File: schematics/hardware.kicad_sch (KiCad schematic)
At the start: 4 parts, among them U1 CR2013-MI2120, U2 TXS0108EPW, U3 BMP280

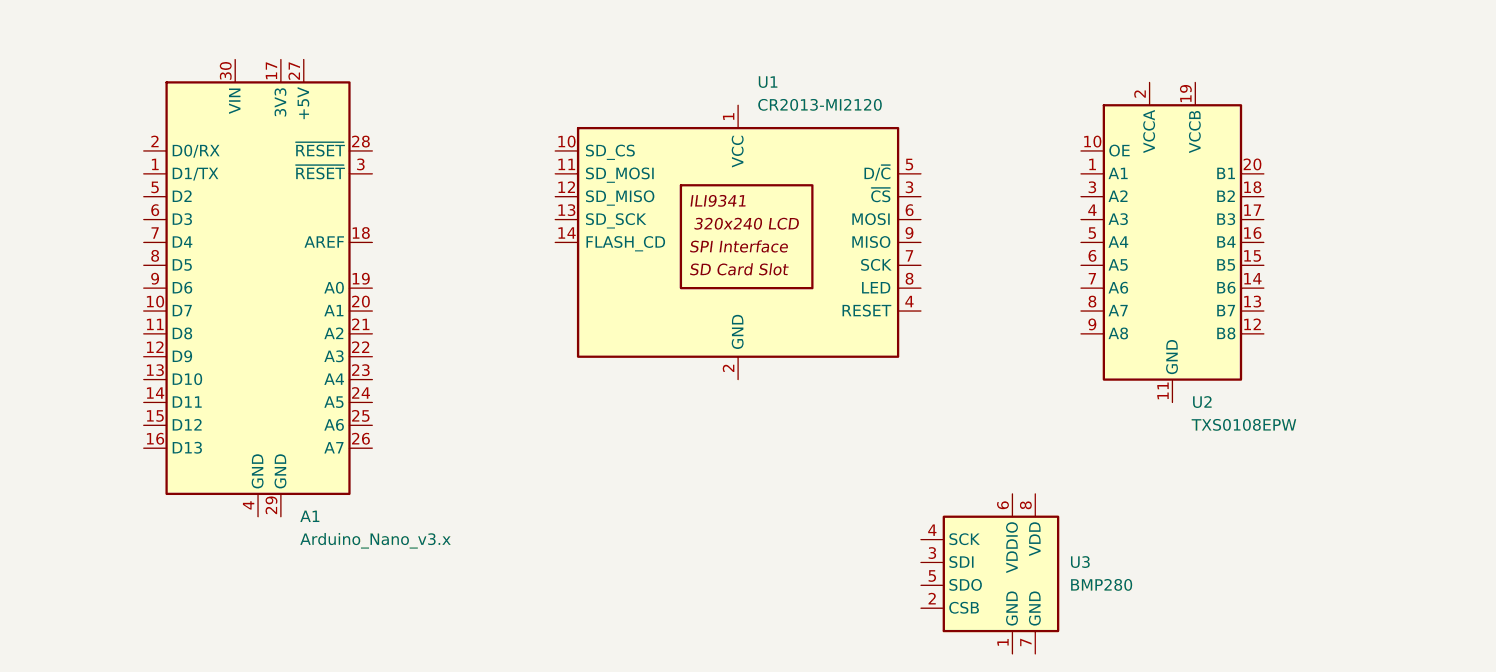
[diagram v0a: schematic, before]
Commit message: finished schematic, pcbnew tbd
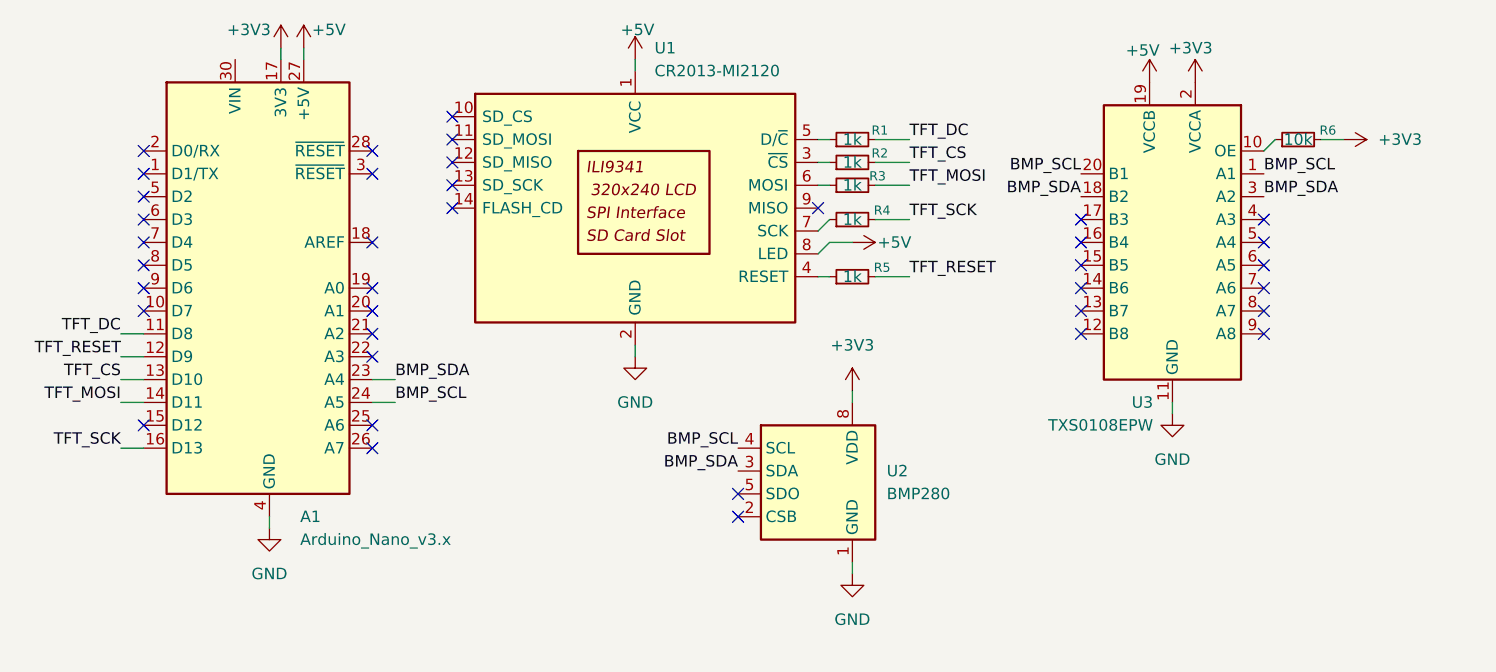
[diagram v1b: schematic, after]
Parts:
- added R1, R2, R3, R4, R5: 1k, Resistor_THT:R_Axial_DIN0207_L6.3mm_D2.5mm_P10.16mm_Horizontal, symbol Device:R_Small
- added R6: 10k, Resistor_THT:R_Axial_DIN0207_L6.3mm_D2.5mm_P10.16mm_Horizontal, symbol Device:R_Small
- renumbered U3 to U2, U2 to U3
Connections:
- net +5V: now reaches U1.1 (VCC)
- net +5V: now also A1.27 (+5V), U1.8 (LED), U3.19 (VCCB)
- net GND: now reaches U1.2 (GND)
- net GND: now also A1.29 (GND), A1.4 (GND), U2.1 (GND), U2.7 (GND), U3.11 (GND)
- net at U1.3 (~{CS}): now also R2.1
- net at U1.4 (RESET): now also R5.1
- net at U1.5 (D/~{C}): now also R1.1
- net at U1.6 (MOSI): now also R3.1
- net at U1.7 (SCK): now also R4.1
- net TFT_DC: now reaches A1.11 (D8)
- net TFT_DC: now also R1.2
- net TFT_RESET: now reaches A1.12 (D9)
- net TFT_RESET: now also R5.2
- net TFT_CS: now reaches A1.13 (D10)
- net TFT_CS: now also R2.2
- net TFT_MOSI: now reaches A1.14 (D11)
- net TFT_MOSI: now also R3.2
- net TFT_SCK: now reaches A1.16 (D13)
- net TFT_SCK: now also R4.2
- net +3V3: now reaches A1.17 (3V3)
- net +3V3: now also U2.6 (VDDIO), U2.8 (VDD), U3.2 (VCCA), R6.2
- net BMP_SDA: now reaches A1.23 (A4)
- net BMP_SDA: now also U2.3 (SDA), U3.18 (B2), U3.3 (A2)
- net BMP_SCL: now reaches A1.24 (A5)
- net BMP_SCL: now also U2.4 (SCL), U3.1 (A1), U3.20 (B1)
- net at U3.10 (OE): now also R6.1
- no-connect marks 0 -> 38
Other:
- moved on the sheet: U1

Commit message: pcbnew done
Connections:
- net BMP_SCL: no longer A1.24 (A5), U3.20 (B1)
- net BMP_SDA: no longer A1.23 (A4), U3.18 (B2)
- new net BMP_SCL_ARD: A1.24 (A5), U3.20 (B1)
- new net BMP_SDA_ARD: A1.23 (A4), U3.18 (B2)
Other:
- moved on the sheet: R6, U3
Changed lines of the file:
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@@
 	)
 	(no_connect
-		(at 175.26 46.99)
+		(at 180.34 48.26)
 	)
 	(no_connect
@@
 	)
 	(no_connect
-		(at 175.26 49.53)
-	)
-	(no_connect
-		(at 154.94 44.45)
+		(at 180.34 50.8)
+	)
+	(no_connect
+		(at 160.02 45.72)
 	)
 	(no_connect
@@
 	)
 	(no_connect
-		(at 154.94 41.91)
+		(at 160.02 43.18)
 	)
 	(no_connect
@@
 	)
 	(no_connect
-		(at 154.94 52.07)
+		(at 160.02 53.34)
 	)
 	(no_connect
@@
 	)
 	(no_connect
-		(at 175.26 44.45)
+		(at 180.34 45.72)
 	)
 	(no_connect
@@
 	)
 	(no_connect
-		(at 154.94 54.61)
+		(at 160.02 55.88)
 	)
 	(no_connect
@@
 	)
 	(no_connect
-		(at 175.26 54.61)
+		(at 180.34 55.88)
 	)
 	(no_connect
@@
 	)
 	(no_connect
-		(at 154.94 46.99)
+		(at 160.02 48.26)
 	)
 	(no_connect
@@
 	)
 	(no_connect
-		(at 175.26 41.91)
+		(at 180.34 43.18)
 	)
 	(no_connect
@@
 	)
 	(no_connect
-		(at 175.26 52.07)
+		(at 180.34 53.34)
 	)
 	(no_connect
@@
 	)
 	(no_connect
-		(at 154.94 49.53)
+		(at 160.02 50.8)
 	)
 	(wire
@@
 	(wire
 		(pts
-			(xy 175.26 34.29) (xy 176.53 33.02)
+			(xy 180.34 35.56) (xy 181.61 34.29)
 		)
 		(stroke
@@
 	(wire
 		(pts
-			(xy 184.15 33.02) (xy 181.61 33.02)
+			(xy 189.23 34.29) (xy 186.69 34.29)
 		)
 		(stroke
@@
 	(wire
 		(pts
-			(xy 165.1 63.5) (xy 165.1 62.23)
+			(xy 170.18 64.77) (xy 170.18 63.5)
 		)
 		(stroke
@@
 		)
 	)
-	(label "BMP_SDA"
+	(label "BMP_SDA_ARD"
 		(at 78.74 59.69 0)
 		(effects
@@
 		)
 	)
-	(label "BMP_SCL"
-		(at 154.94 36.83 180)
+	(label "BMP_SCL_ARD"
+		(at 160.02 38.1 180)
 		(effects
 			(font
@@
 	)
 	(label "BMP_SCL"
-		(at 175.26 36.83 0)
+		(at 180.34 38.1 0)
 		(effects
 			(font
@@
 		)
 	)
-	(label "BMP_SCL"
+	(label "BMP_SCL_ARD"
 		(at 78.74 62.23 0)
 		(effects
@@
 	)
 	(label "BMP_SDA"
-		(at 175.26 39.37 0)
+		(at 180.34 40.64 0)
 		(effects
 			(font
@@
 		)
 	)
-	(label "BMP_SDA"
-		(at 154.94 39.37 180)
+	(label "BMP_SDA_ARD"
+		(at 160.02 40.64 180)
 		(effects
 			(font
@@
 	(symbol
 		(lib_id "power:+5V")
-		(at 162.56 26.67 0)
+		(at 167.64 27.94 0)
 		(unit 1)
 		(exclude_from_sim no)
@@
 		(dnp no)
 		(property "Reference" "#PWR09"
-			(at 162.56 30.48 0)
+			(at 167.64 31.75 0)
 			(effects
 				(font
@@
 		)
 		(property "Value" "+5V"
-			(at 161.798 23.114 0)
+			(at 166.878 24.384 0)
 			(effects
 				(font
@@
 		)
 		(property "Footprint" ""
-			(at 162.56 26.67 0)
+			(at 167.64 27.94 0)
 			(effects
 				(font
@@
 		)
 		(property "Datasheet" ""
-			(at 162.56 26.67 0)
+			(at 167.64 27.94 0)
 			(effects
 				(font
@@
 		)
 		(property "Description" "Power symbol creates a global label with name \"+5V\""
-			(at 162.56 26.67 0)
+			(at 167.64 27.94 0)
 			(effects
 				(font
@@
 	(symbol
 		(lib_id "power:+3V3")
-		(at 167.64 26.67 0)
+		(at 172.72 27.94 0)
 		(unit 1)
 		(exclude_from_sim no)
@@
 		(dnp no)
 		(property "Reference" "#PWR011"
-			(at 167.64 30.48 0)
+			(at 172.72 31.75 0)
 			(effects
 				(font
@@
 		)
 		(property "Value" "+3V3"
-			(at 167.132 22.86 0)
+			(at 172.212 24.13 0)
 			(effects
 				(font
@@
 		)
 		(property "Footprint" ""
-			(at 167.64 26.67 0)
+			(at 172.72 27.94 0)
 			(effects
 				(font
@@
 		)
 		(property "Datasheet" ""
-			(at 167.64 26.67 0)
+			(at 172.72 27.94 0)
 			(effects
 				(font
@@
 		)
 		(property "Description" "Power symbol creates a global label with name \"+3V3\""
-			(at 167.64 26.67 0)
+			(at 172.72 27.94 0)
 			(effects
 				(font
@@
 	(symbol
 		(lib_id "power:+3V3")
-		(at 184.15 33.02 270)
+		(at 189.23 34.29 270)
 		(unit 1)
 		(exclude_from_sim no)
@@
 		(fields_autoplaced yes)
 		(property "Reference" "#PWR012"
-			(at 180.34 33.02 0)
+			(at 185.42 34.29 0)
 			(effects
 				(font
@@
 		)
 		(property "Value" "+3V3"
-			(at 187.96 33.0199 90)
+			(at 193.04 34.2899 90)
 			(effects
 				(font
@@
 		)
 		(property "Footprint" ""
-			(at 184.15 33.02 0)
+			(at 189.23 34.29 0)
 			(effects
 				(font
@@
 		)
 		(property "Datasheet" ""
-			(at 184.15 33.02 0)
+			(at 189.23 34.29 0)
 			(effects
 				(font
@@
 		)
 		(property "Description" "Power symbol creates a global label with name \"+3V3\""
-			(at 184.15 33.02 0)
+			(at 189.23 34.29 0)
 			(effects
 				(font
@@
 	(symbol
 		(lib_id "power:GND")
-		(at 165.1 63.5 0)
+		(at 170.18 64.77 0)
 		(unit 1)
 		(exclude_from_sim no)
@@
 		(fields_autoplaced yes)
 		(property "Reference" "#PWR010"
-			(at 165.1 69.85 0)
+			(at 170.18 71.12 0)
 			(effects
 				(font
@@
 		)
 		(property "Value" "GND"
-			(at 165.1 68.58 0)
+			(at 170.18 69.85 0)
 			(effects
 				(font
@@
 		)
 		(property "Footprint" ""
-			(at 165.1 63.5 0)
+			(at 170.18 64.77 0)
 			(effects
 				(font
@@
 		)
 		(property "Datasheet" ""
-			(at 165.1 63.5 0)
+			(at 170.18 64.77 0)
 			(effects
 				(font
@@
 		)
 		(property "Description" "Power symbol creates a global label with name \"GND\" , ground"
-			(at 165.1 63.5 0)
+			(at 170.18 64.77 0)
 			(effects
 				(font
@@
 	(symbol
 		(lib_id "Logic_LevelTranslator:TXS0108EPW")
-		(at 165.1 44.45 0)
+		(at 170.18 45.72 0)
 		(mirror y)
 		(unit 1)
@@
 		(dnp no)
 		(property "Reference" "U3"
-			(at 162.9567 62.23 0)
+			(at 168.0367 63.5 0)
 			(effects
 				(font
@@
 		)
 		(property "Value" "TXS0108EPW"
-			(at 162.9567 64.77 0)
+			(at 168.0367 66.04 0)
 			(effects
 				(font
@@
 		)
 		(property "Footprint" "Package_SO:TSSOP-20_4.4x6.5mm_P0.65mm"
-			(at 165.1 63.5 0)
+			(at 170.18 64.77 0)
 			(effects
 				(font
@@
 		)
 		(property "Datasheet" "www.ti.com/lit/ds/symlink/txs0108e.pdf"
-			(at 165.1 46.99 0)
+			(at 170.18 48.26 0)
 			(effects
 				(font
@@
 		)
 		(property "Description" "Bidirectional  level-shifting voltage translator, TSSOP-20"
-			(at 165.1 44.45 0)
+			(at 170.18 45.72 0)
 			(effects
 				(font
@@
 	(symbol
 		(lib_id "Device:R_Small")
-		(at 179.07 33.02 90)
+		(at 184.15 34.29 90)
 		(unit 1)
 		(exclude_from_sim no)
@@
 		(dnp no)
 		(property "Reference" "R6"
-			(at 182.372 32.004 90)
+			(at 187.452 33.274 90)
 			(effects
 				(font
@@
 		)
 		(property "Value" "10k"
-			(at 179.07 33.02 90)
+			(at 184.15 34.29 90)
 			(effects
 				(font
@@
 		)
 		(property "Footprint" "Resistor_THT:R_Axial_DIN0207_L6.3mm_D2.5mm_P10.16mm_Horizontal"
-			(at 179.07 33.02 0)
+			(at 184.15 34.29 0)
 			(effects
 				(font
@@
 		)
 		(property "Datasheet" "~"
-			(at 179.07 33.02 0)
+			(at 184.15 34.29 0)
 			(effects
 				(font
@@
 		)
 		(property "Description" "Resistor, small symbol"
-			(at 179.07 33.02 0)
-			(effects
-				(font
+			(at 184.15 34.29 0)
+			(effects
+				(font
